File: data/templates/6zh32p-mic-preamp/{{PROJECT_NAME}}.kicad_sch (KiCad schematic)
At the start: 9 parts, among them X1 6ZH32P

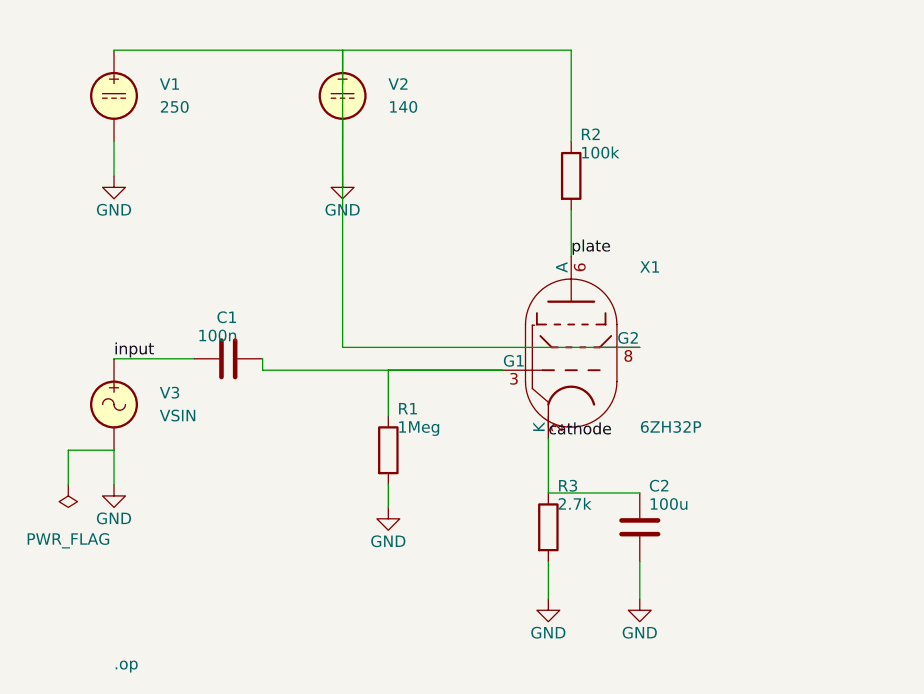
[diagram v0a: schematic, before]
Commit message: T187 Phase 4: 3 T031 builders + regen 11/11 + acceptance + ADR + CHANGELOG
Pentode SE-resistive parametric builder
(tests/integration/adapters/schematic_kicad/test_pentode_se_resistive_facade.py):
restores Python source-of-truth for 3 T031 templates historically
built by one-shot /tmp/build_t031_templates.py (not committed).
NamedTuple _PentodeParams + shared _build_pentode_se_resistive helper +
3 thin wrappers (_build_6p13s_se_resistive / _build_6zh32p_mic_preamp /
_build_6zh38p_if_amp).

Routing edge case: V_BB/V_G2 power-source positions create a
3-wire endpoint coincidence at pin_plus when connect() uses default
vertical-first Manhattan (corner = (start.x, end.y) lands exactly on
pin_plus → KiCad short). Builder routes horizontal-first through
(R_a.x, V_BB.pin_minus.y) to avoid V_BB.pin_plus midpoint collision.
Documented inline in builder + ADR-T187a consequences section.

scripts/regenerate-templates.py: 3 new _import_*_builder + shared
_bake_pentode_se_resistive helper + 3 new thin _bake_* + entries in
_BAKERS. template.yaml content preserved verbatim from baked
artefacts. README.md regenerated with builder cross-ref.

Regenerated all 11 templates. ERC verification (kicad-cli sch erc
--format json):
- 6p13s-se-resistive: off-grid=0, errors=0
- 6zh32p-mic-preamp: off-grid=0, errors=0
- 6zh38p-if-amp:     off-grid=0, errors=0
- op-amp-inverting:  off-grid=0, errors=0
- bjt-ce-nfb:        off-grid=0, errors=0
- active-lpf-sallen-key: off-grid=0, errors=0
- (5 already-clean templates: unchanged, still 0/0)

`efactory design check-grid` smoke 11/11 → "0 off-grid endpoints. ✓"
(SC2 PASSED).

T031 numerical acceptance (tests/integration/composition/
test_t031_phase5_templates.py) — 3/3 PASSED:
- 6P13S V(plate)=65.7V ∈ [40,120]; Ia/Ig2 in bounds
- 6ZH32P V(plate) ∈ [60,110]V; Ia ∈ [1.0,2.5]mA
- 6ZH38P V(plate) ∈ [80,140]V; Ia ∈ [2.5,5.0]mA
(SC3 PASSED — numerical-identical bit-equiv via per-node-name
remapping per Analyze W2).

DECISIONS.md: ADR-T187a (snap-on-write 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
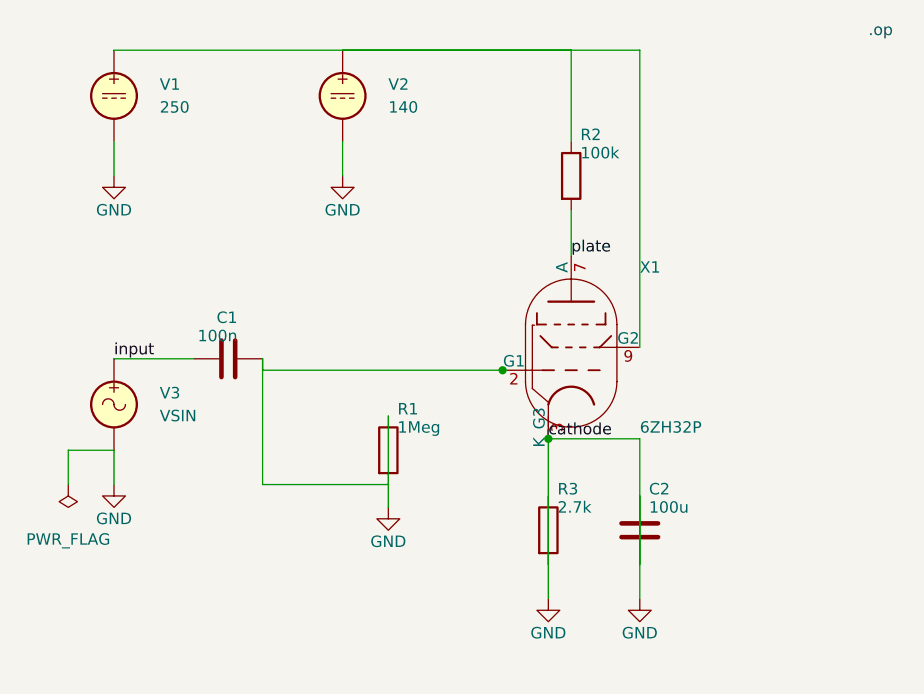
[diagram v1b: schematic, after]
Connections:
- net GND: now also C2.1, R1.1, R3.1, X1.3 (K_G3); no longer R1.2, V2.1, X1.8 (G2)
- net plate: now also X1.7 (A); no longer X1.6 (A)
- net at R2.1, V1.1: now also V2.1, X1.9 (G2)
- removed net cathode: C2.1, R3.1, X1.2 (K)
- new net: C1.2, R1.2, X1.2 (G1)
